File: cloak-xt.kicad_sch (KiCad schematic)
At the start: 16 parts, among them J1 JST, U1 STM32F072CBT6

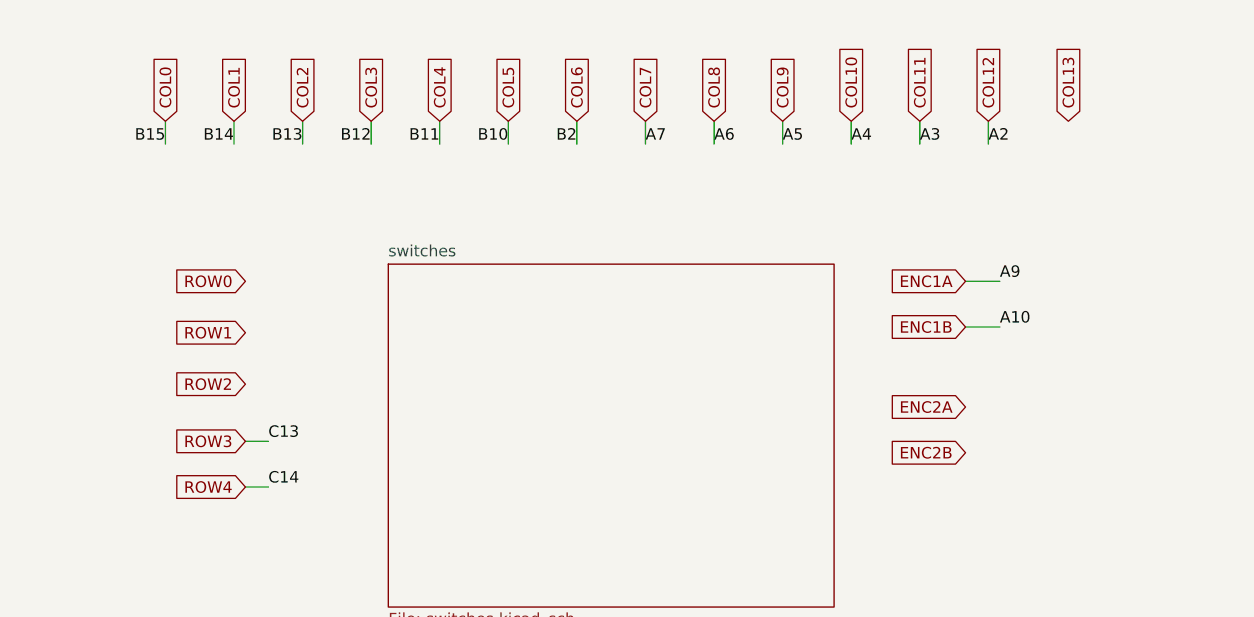
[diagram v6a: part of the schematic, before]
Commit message: Complete initial PCB
Complete PCB traces with matrix and ground planes. No GND vias yet.
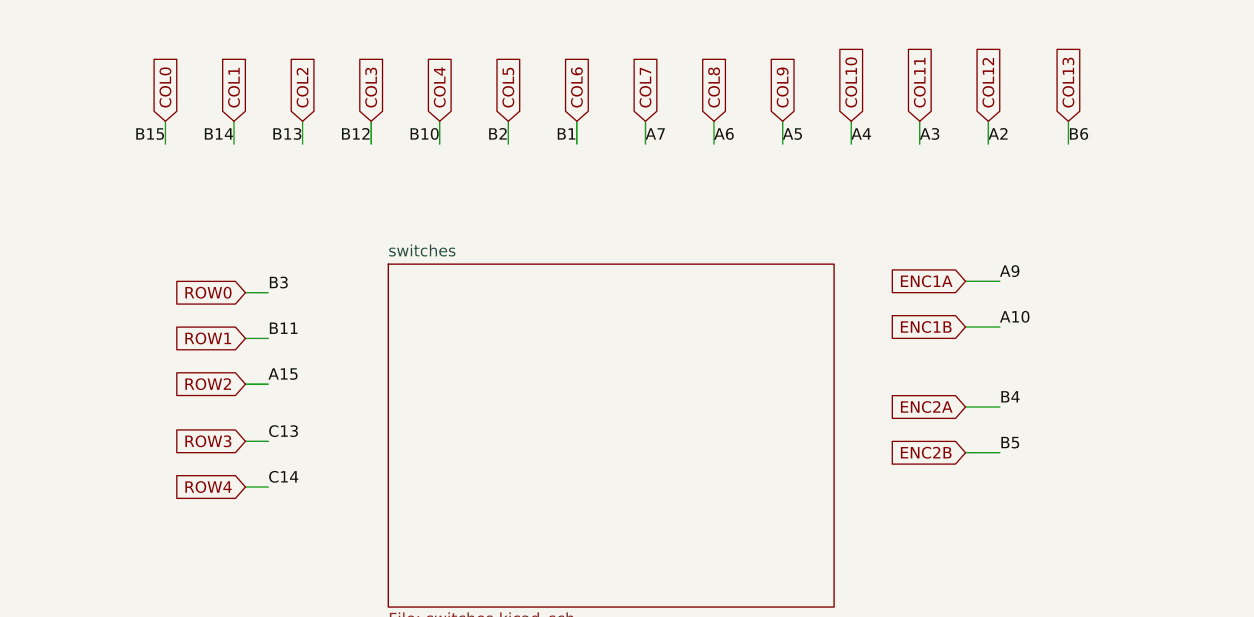
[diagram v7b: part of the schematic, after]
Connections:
- net A15 is gone; now on net ROW2: U1.38 (PA15)
- net B1 is gone; now on net COL6: U1.19 (PB1)
- net B3 is gone; now on net ROW0: U1.39 (PB3)
- net B4 is gone; now on net ENC2A: U1.40 (PB4)
- net B5 is gone; now on net ENC2B: U1.41 (PB5)
- net B6 is gone; now on net COL13: U1.42 (PB6)
- net COL4: now also U1.21 (PB10); no longer U1.22 (PB11)
- net COL5: now also U1.20 (PB2); no longer U1.21 (PB10)
- net COL6: no longer U1.20 (PB2)
- net ROW1: now also U1.22 (PB11)
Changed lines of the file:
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@@
+	(wire
+		(pts
+			(xy 270.51 30.48) (xy 270.51 33.02)
+		)
+		(stroke
+			(width 0)
+			(type default)
+		)
+	)
 	(wire
 		(pts
@@
 	(wire
 		(pts
+			(xy 259.08 62.23) (xy 262.89 62.23)
+		)
+		(stroke
+			(width 0)
+			(type default)
+		)
+	)
+	(wire
+		(pts
 			(xy 246.38 30.48) (xy 246.38 33.02)
 		)
@@
 	(wire
 		(pts
+			(xy 259.08 67.31) (xy 262.89 67.31)
+		)
+		(stroke
+			(width 0)
+			(type default)
+		)
+	)
+	(wire
+		(pts
 			(xy 99.695 58.42) (xy 97.155 58.42)
 		)
@@
 	(wire
 		(pts
+			(xy 179.07 59.69) (xy 181.61 59.69)
+		)
+		(stroke
+			(width 0)
+			(type default)
+		)
+	)
+	(wire
+		(pts
 			(xy 103.505 57.785) (xy 99.695 57.785)
 		)
@@
 	(wire
 		(pts
+			(xy 179.07 54.61) (xy 181.61 54.61)
+		)
+		(stroke
+			(width 0)
+			(type default)
+		)
+	)
+	(wire
+		(pts
 			(xy 149.225 186.055) (xy 136.525 186.055)
 		)
@@
 			(width 0)
 			(type solid)
+		)
+	)
+	(wire
+		(pts
+			(xy 179.07 49.53) (xy 181.61 49.53)
+		)
+		(stroke
+			(width 0)
+			(type default)
 		)
 	)
@@
 		)
 	)
+	(label "B1"
+		(at 215.9 33.02 180)
+		(fields_autoplaced yes)
+		(effects
+			(font
+				(size 1.27 1.27)
+			)
+			(justify right bottom)
+		)
+	)
 	(label "A3"
 		(at 98.425 38.1 0)
@@
 	)
 	(label "B10"
-		(at 208.28 33.02 180)
+		(at 200.66 33.02 180)
 		(fields_autoplaced yes)
 		(effects
@@
 		)
 	)
+	(label "B3"
+		(at 181.61 49.53 0)
+		(fields_autoplaced yes)
+		(effects
+			(font
+				(size 1.27 1.27)
+			)
+			(justify left bottom)
+		)
+	)
 	(label "A2"
 		(at 98.425 35.56 0)
@@
 		)
 	)
+	(label "B6"
+		(at 270.51 33.02 0)
+		(fields_autoplaced yes)
+		(effects
+			(font
+				(size 1.27 1.27)
+			)
+			(justify left bottom)
+		)
+	)
 	(label "B15"
 		(at 60.96 96.52 180)
@@
 	)
 	(label "B11"
-		(at 200.66 33.02 180)
-		(fields_autoplaced yes)
-		(effects
-			(font
-				(size 1.27 1.27)
-			)
-			(justify right bottom)
+		(at 181.61 54.61 0)
+		(fields_autoplaced yes)
+		(effects
+			(font
+				(size 1.27 1.27)
+			)
+			(justify left bottom)
 		)
 	)
@@
 		)
 	)
+	(label "A15"
+		(at 181.61 59.69 0)
+		(fields_autoplaced yes)
+		(effects
+			(font
+				(size 1.27 1.27)
+			)
+			(justify left bottom)
+		)
+	)
 	(label "B10"
 		(at 60.96 83.82 180)
@@
 		)
 	)
+	(label "B5"
+		(at 262.89 67.31 0)
+		(fields_autoplaced yes)
+		(effects
+			(font
+				(size 1.27 1.27)
+			)
+			(justify left bottom)
+		)
+	)
 	(label "A2"
 		(at 261.62 33.02 0)
@@
 	)
 	(label "B2"
-		(at 215.9 33.02 180)
-		(fields_autoplaced yes)
-		(effects
-			(font
-				(size 1.27 1.27)
-			)
-			(justify right bottom)
+		(at 208.28 33.02 180)
+		(fields_autoplaced yes)
+		(effects
+			(font
+				(size 1.27 1.27)
+			)
+			(justify right bottom)
+		)
+	)
+	(label "B4"
+		(at 262.89 62.23 0)
+		(fields_autoplaced yes)
+		(effects
+			(font
+				(size 1.27 1.27)
+			)
+			(justify left bottom)
 		)
 	)
@@
 	(global_label "ROW1"
 		(shape input)
-		(at 179.07 53.975 180)
+		(at 179.07 54.61 180)
 		(fields_autoplaced yes)
 		(effects
@@
 		)
 		(property "Intersheetrefs" "${INTERSHEET_REFS}"
-			(at 170.9028 53.975 0)
+			(at 170.9028 54.61 0)
 			(effects
 				(font
@@
 	(global_label "ROW0"
 		(shape input)
-		(at 179.07 48.26 180)
+		(at 179.07 49.53 180)
 		(fields_autoplaced yes)
 		(effects
@@
 		)
 		(property "Intersheetrefs" "${INTERSHEET_REFS}"
-			(at 170.9028 48.26 0)
+			(at 170.9028 49.53 0)
 			(effects
 				(font

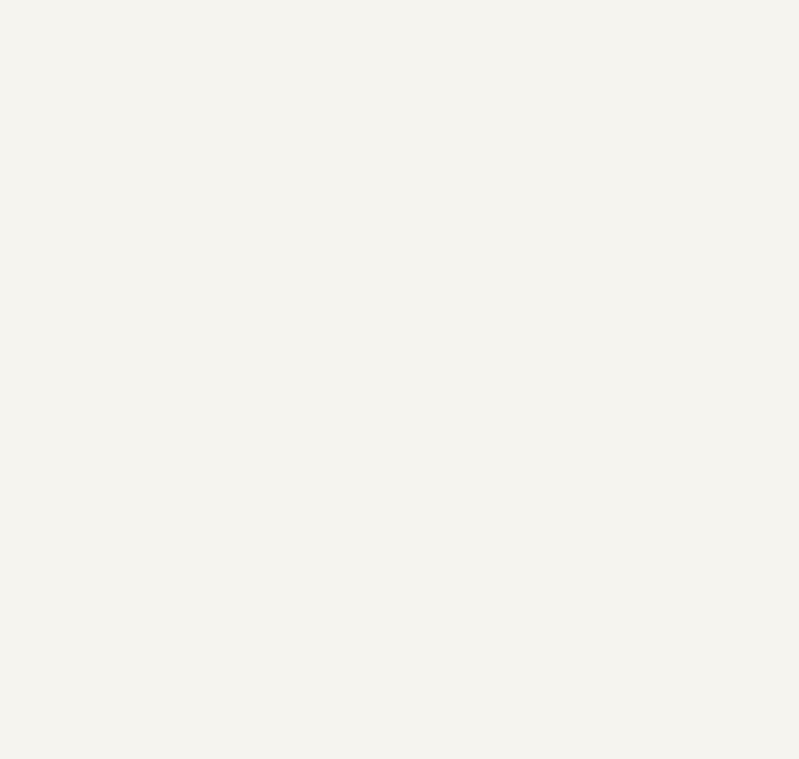
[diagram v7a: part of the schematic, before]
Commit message: Add schematics for SK6812MINI-E on Capslock/Stepped
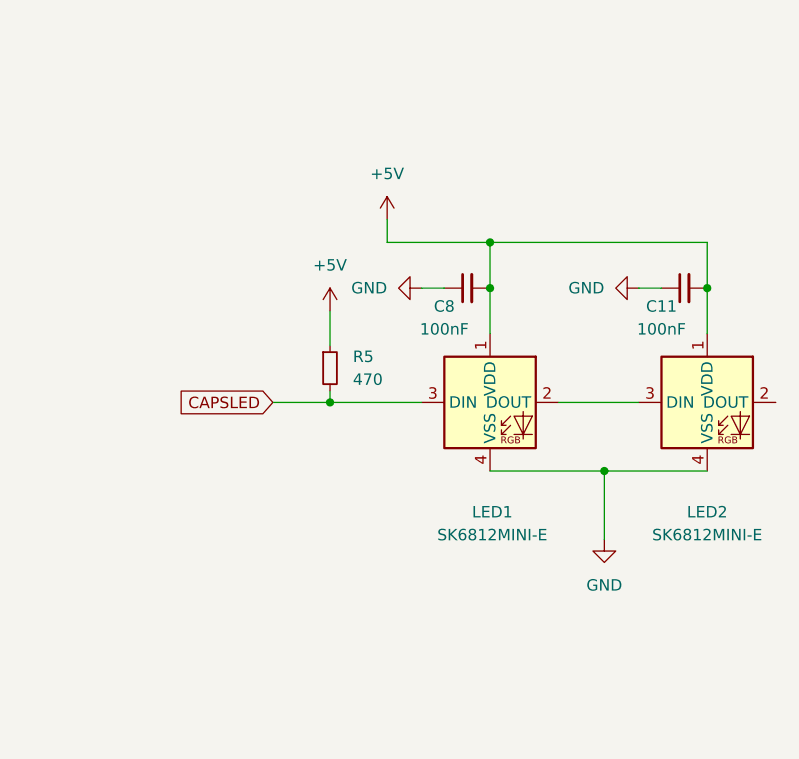
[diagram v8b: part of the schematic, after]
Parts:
- added C11, C8: 100nF, Capacitor_SMD:C_0402_1005Metric, symbol Device:C_Small
- added LED1, LED2: SK6812MINI-E, PCM_marbastlib-various:LED_6028R, symbol PCM_marbastlib-various:SK6812MINI-E
- added R5: 470, Resistor_SMD:R_0402_1005Metric, symbol Device:R_Small
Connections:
- net +5V: now also C11.2, C8.2, LED1.1 (VDD), LED2.1 (VDD), R5.1
- net GND: now also C11.1, C8.1, LED1.4 (VSS), LED2.4 (VSS)
- new net: LED1.2 (DOUT), LED2.3 (DIN)
- new net CAPSLED: LED1.3 (DIN), R5.2
